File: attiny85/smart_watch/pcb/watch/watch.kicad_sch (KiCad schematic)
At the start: 20 parts, among them J1 Display, J2 USB C, SW1 Wake, SW2 Select, SW3 Set, SW4 Reset, U1 ATTINY85, U2 MCP73831-2-OT

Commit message: production files
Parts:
- removed BT1: Battery_Cell, Battery:BatteryHolder_Keystone_1058_1x2032, symbol Device:Battery_Cell
- added BT1: 1059, BatteryHolder_Keystone_1059_THT:BatteryHolder_Keystone_1059_THT, symbol BatteryHolder_Keystone_1059:1059
- added J3: LiPo Batt, Connector_JST:JST_PH_S2B-PH-K_1x02_P2.00mm_Horizontal, symbol Connector:Conn_01x02_Pin
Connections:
- net GND: now also BT1.N, J3.2 (Pin_2)
- net VCC: now also BT1.P1, J3.1 (Pin_1)
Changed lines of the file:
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@@
+		)
+	)
+	(global_label "GND"
+		(shape bidirectional)
+		(at 105.5509 99.8584 270)
+		(effects
+			(font
+				(size 0.7 0.7)
+			)
+			(justify right)
+		)
+		(property "Intersheetrefs" "${INTERSHEET_REFS}"
+			(at 105.5509 99.8584 0)
+			(effects
+				(font
+					(size 1.27 1.27)
+				)
+				(hide yes)
+			)
 		)
 	)
@@
 		)
 	)
+	(global_label "GND"
+		(shape bidirectional)
+		(at 115.57 95.25 90)
+		(effects
+			(font
+				(size 0.7 0.7)
+			)
+			(justify left)
+		)
+		(property "Intersheetrefs" "${INTERSHEET_REFS}"
+			(at 115.57 95.25 90)
+			(effects
+				(font
+					(size 1.27 1.27)
+				)
+				(hide yes)
+			)
+		)
+	)
 	(global_label "WAKE"
 		(shape output)
@@
 		)
 	)
+	(global_label "VCC"
+		(shape bidirectional)
+		(at 105.556 93.8939 90)
+		(effects
+			(font
+				(size 0.7 0.7)
+			)
+			(justify left)
+		)
+		(property "Intersheetrefs" "${INTERSHEET_REFS}"
+			(at 105.556 93.8939 0)
+			(effects
+				(font
+					(size 1.27 1.27)
+				)
+				(hide yes)
+			)
+		)
+	)
 	(global_label "GND"
 		(shape bidirectional)
@@
 		)
 	)
-	(global_label "VCC"
-		(shape bidirectional)
-		(at 106.68 92.71 90)
-		(effects
-			(font
-				(size 0.7 0.7)
-			)
-			(justify left)
-		)
-		(property "Intersheetrefs" "${INTERSHEET_REFS}"
-			(at 106.68 92.71 0)
-			(effects
-				(font
-					(size 1.27 1.27)
-				)
-				(hide yes)
-			)
-		)
-	)
 	(global_label "SELECT"
 		(shape input)
@@
 		(property "Intersheetrefs" "${INTERSHEET_REFS}"
 			(at 153.67 81.28 0)
-			(effects
-				(font
-					(size 1.27 1.27)
-				)
-				(hide yes)
-			)
-		)
-	)
-	(global_label "GND"
-		(shape bidirectional)
-		(at 106.68 100.33 270)
-		(effects
-			(font
-				(size 0.7 0.7)
-			)
-			(justify right)
-		)
-		(property "Intersheetrefs" "${INTERSHEET_REFS}"
-			(at 106.68 100.33 0)
 			(effects
 				(font
@@
 				)
 				(justify left)
+				(hide yes)
+			)
+		)
+	)
+	(global_label "VCC"
+		(shape bidirectional)
+		(at 113.03 95.25 90)
+		(effects
+			(font
+				(size 0.7 0.7)
+			)
+			(justify left)
+		)
+		(property "Intersheetrefs" "${INTERSHEET_REFS}"
+			(at 113.03 95.25 90)
+			(effects
+				(font
+					(size 1.27 1.27)
+				)
 				(hide yes)
 			)
@@
 	)
 	(symbol
+		(lib_id "BatteryHolder_Keystone_1059:1059")
+		(at 105.556 97.7039 270)
+		(unit 1)
+		(exclude_from_sim no)
+		(in_bom yes)
+		(on_board yes)
+		(dnp yes)
+		(property "Reference" "BT1"
+			(at 97.428 95.4179 90)
+			(effects
+				(font
+					(size 1.27 1.27)
+				)
+				(justify left)
+			)
+		)
+		(property "Value" "1059"
+			(at 97.428 97.9579 90)
+			(effects
+				(font
+					(size 1.27 1.27)
+				)
+				(justify left)
+			)
+		)
+		(property "Footprint" "BatteryHolder_Keystone_1059_THT:BatteryHolder_Keystone_1059_THT"
+			(at 94.888 97.4499 0)
+			(effects
+				(font
+					(size 1.27 1.27)
+				)
+				(justify bottom)
+				(hide yes)
+			)
+		)
+		(property "Datasheet" ""
+			(at 105.556 97.7039 0)
+			(effects
+				(font
+					(size 1.27 1.27)
+				)
+				(hide yes)
+			)
+		)
+		(property "Description" "Keystone Electronics Coin Cell holder 1059"
+			(at 98.698 95.4179 0)
+			(effects
+				(font
+					(size 1.27 1.27)
+				)
+				(hide yes)
+			)
+		)
+		(pin "N"
+		)
+		(pin "P1"
+		)
+		(pin "P2"
+		)
+		(instances
+			(project ""
+				(path "/552443dc-5cb6-43cc-861c-1c1d9f5bdc51"
+					(reference "BT1")
+					(unit 1)
+				)
+			)
+		)
+	)
+	(symbol
 		(lib_id "Device:R")
 		(at 127 133.35 180)
@@
 	)
 	(symbol
-		(lib_id "Device:Battery_Cell")
-		(at 106.68 97.79 0)
-		(unit 1)
-		(exclude_from_sim no)
-		(in_bom yes)
-		(on_board yes)
-		(dnp no)
-		(fields_autoplaced yes)
-		(property "Reference" "BT1"
-			(at 110.49 94.6784 0)
-			(effects
-				(font
-					(size 1.27 1.27)
-				)
-				(justify left)
-			)
-		)
-		(property "Value" "Battery_Cell"
-			(at 110.49 97.2184 0)
-			(effects
-				(font
-					(size 1.27 1.27)
-				)
-				(justify left)
-			)
-		)
-		(property "Footprint" "Battery:BatteryHolder_Keystone_1058_1x2032"
-			(at 106.68 96.266 90)
-			(effects
-				(font
-					(size 1.27 1.27)
-				)
-				(hide yes)
-			)
-		)
-		(property "Datasheet" "~"
-			(at 106.68 96.266 90)
-			(effects
-				(font
-					(size 1.27 1.27)
-				)
-				(hide yes)
-			)
-		)
-		(property "Description" "Single-cell battery"
-			(at 106.68 97.79 0)
-			(effects
-				(font
-					(size 1.27 1.27)
-				)
-				(hide yes)
-			)
-		)
-		(pin "2"
-		)
-		(pin "1"
-		)
-		(instances
-			(project ""
-				(path "/552443dc-5cb6-43cc-861c-1c1d9f5bdc51"
-					(reference "BT1")
-					(unit 1)
-				)
-			)
-		)
-	)
-	(symbol
 		(lib_id "Connector:USB_C_Receptacle_PowerOnly_6P")
 		(at 151.13 124.46 0)
@@
 					(unit 1)
 				)
+			)
+		)
+	)
+	(symbol
+		(lib_id "Connector:Conn_01x02_Pin")
+		(at 113.03 100.33 90)
+		(unit 1)
+		(exclude_from_sim no)
+		(in_bom yes)
+		(on_board yes)
+		(dnp yes)
+		(property "Reference" "J3"
+			(at 114.1866 101.758 90)
+			(effects
+				(font
+					(size 1.27 1.27)
+				)
+			)
+		)
+		(property "Value" "LiPo Batt"
+			(at 114.046 104.394 90)
+			(effects
+				(font
+					(size 1.27 1.27)
+				)
+			)
+		)
+		(property "Footprint" "Connector_JST:JST_PH_S2B-PH-K_1x02_P2.00mm_Horizontal"
+			(at 113.03 100.33 0)
+			(effects
+				(font
+					(size 1.27 1.27)
+				)
+				(hide yes)
+			)
+		)
+		(property "Datasheet" "~"
+			(at 113.03 100.33 0)
+			(effects
+				(font
+					(size 1.27 1.27)
+				)
+				(hide yes)
+			)
+		)
+		(property "Description" "Generic connector, single row, 01x02, script generated"
+			(at 113.03 100.33 0)
+			(effects
+				(font
+					(size 1.27 1.27)
+				)
+				(hide yes)
+			)
+		)
+		(pin "2"
+		)
+		(pin "1"
+		)
+		(instances
+			(project ""
+				(path "/552443dc-5cb6-43cc-861c-1c1d9f5bdc51"
+					(reference "J3")
+					(unit 1)
+				)

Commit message: added programming connection
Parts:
- removed BT1: 1059, BatteryHolder_Keystone_1059_THT:BatteryHolder_Keystone_1059_THT, symbol BatteryHolder_Keystone_1059:1059
- removed J3: LiPo Batt, Connector_JST:JST_PH_S2B-PH-K_1x02_P2.00mm_Horizontal, symbol Connector:Conn_01x02_Pin
- added BT1: Battery_Cell, Battery:BatteryHolder_Keystone_1060_1x2032, symbol Device:Battery_Cell
- added J3: Programmer, JST_PH_1x06_2mm_horizontal:JST_PH_1x06_2mm_horizontal.pretty, symbol JST_PH_1x06_2mm_horizontal:S6B-PH-SM4-TB_LF__SN_
- added P1: JST_LIPO, JST_PH_1x02_2mm_horizontal:JST_PH_1x02_2mm_horizontal, symbol JST_PH_1x02_2mm_horizontal:S2B-PH-SM4-TB_LF__SN_
- R3: value 3.6k -> 6.8k
- SW1, SW2, SW3, SW4: footprint Button_Switch_THT:SW_TH_Tactile_Omron_B3F-100x -> Button_Switch_SMD:SW_SPST_Omron_B3FS-101xP
- U1: footprint Package_DIP:DIP-8_W7.62mm -> Package_DIP:DIP-8_W7.62mm_SMDSocket_SmallPads
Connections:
- net GND: now also BT1.2 (-), J3.5, P1.2
- net RESET: now also J3.6
- net SCK: now also J3.4
- net VCC: now also BT1.1 (+), J3.1, P1.1
- net SDA renamed MOSI
- net MOSI: now also J3.3
- net WAKE renamed MISO
- net MISO: now also J3.2
- new net: J3.S1 (SHIELD), J3.S2 (SHIELD)
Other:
- note added: "Programming"

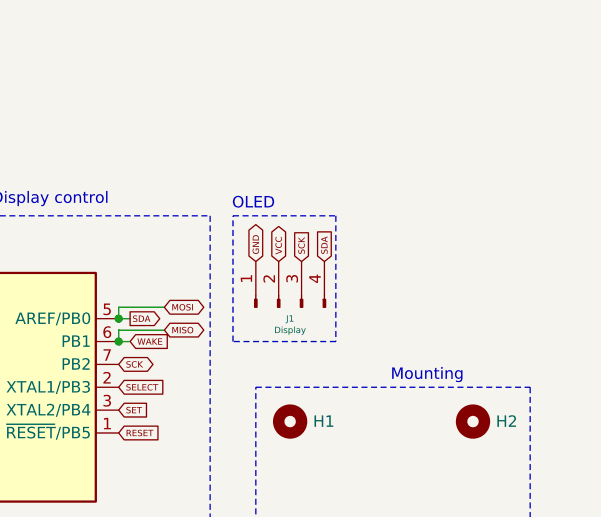
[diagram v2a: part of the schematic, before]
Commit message: watch with straps
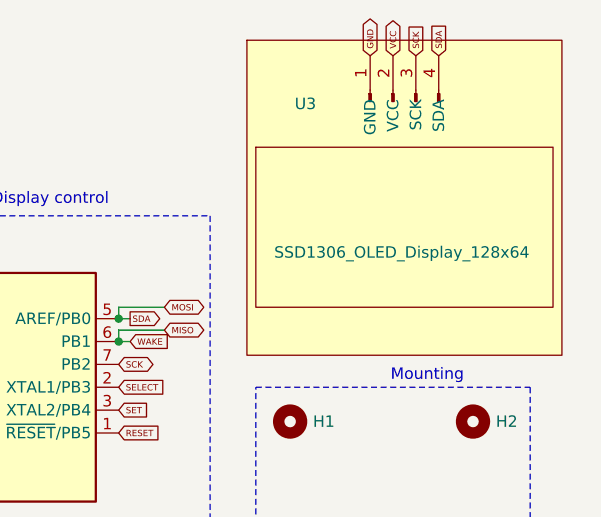
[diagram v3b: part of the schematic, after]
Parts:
- removed J1: Display, Connector_PinHeader_2.54mm:PinHeader_1x04_P2.54mm_Vertical, symbol Connector:Conn_01x04_Pin
- added U3: SSD1306_OLED_Display_128x64, My_Footprints:SSD1306_OLED_Display_128x64, symbol My_Symbols:SSD1306_OLED_Display_128x64
- H1, H2, H3, H4: footprint MountingHole:MountingHole_2.1mm -> My_Footprints:Circular_Mounting_Hole_1mmDia
- J2: footprint Connector_USB:USB_C_Receptacle_HRO_TYPE-C-31-M-17 -> Connector_USB:USB_C_Receptacle_GCT_USB4125-xx-x-0190_6P_TopMnt_Horizontal
- SW1, SW2, SW3, SW4: footprint Button_Switch_SMD:SW_SPST_Omron_B3FS-101xP -> Button_Switch_SMD:SW_Tactile_SPST_NO_Straight_CK_PTS636Sx25SMTRLFS
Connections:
- net GND: now also U3.1 (GND)
- net MOSI: now also U3.4 (SDA)
- net SCK: now also U3.3 (SCK)
- net VCC: now also U3.2 (VCC)
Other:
- note removed: "OLED"
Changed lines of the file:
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@@
-	)
-	(rectangle
-		(start 166.37 62.23)
-		(end 177.8 76.2)
-		(stroke
-			(width 0)
-			(type dash)
-		)
-		(fill
-			(type none)
-		)
 	)
 	(rectangle
@@
 		)
 	)
-	(text "OLED"
-		(exclude_from_sim no)
-		(at 168.656 60.96 0)
-		(effects
-			(font
-				(size 1.27 1.27)
-			)
-		)
-	)
 	(text "MCU: Clock and Display control"
 		(exclude_from_sim no)
@@
 		)
 	)
-	(global_label "SDA"
-		(shape input)
-		(at 176.53 67.31 90)
-		(effects
-			(font
-				(size 0.7 0.7)
-			)
-			(justify left)
-		)
-		(property "Intersheetrefs" "${INTERSHEET_REFS}"
-			(at 176.53 67.31 0)
-			(effects
-				(font
-					(size 1.27 1.27)
-				)
-				(hide yes)
-			)
-		)
-	)
 	(global_label "GND"
 		(shape bidirectional)
@@
 		)
 	)
+	(global_label "SCK"
+		(shape input)
+		(at 186.69 44.45 90)
+		(effects
+			(font
+				(size 0.7 0.7)
+			)
+			(justify left)
+		)
+		(property "Intersheetrefs" "${INTERSHEET_REFS}"
+			(at 186.69 44.45 0)
+			(effects
+				(font
+					(size 1.27 1.27)
+				)
+				(hide yes)
+			)
+		)
+	)
 	(global_label "SET"
 		(shape input)
@@
 		(property "Intersheetrefs" "${INTERSHEET_REFS}"
 			(at 173.99 129.54 0)
+			(effects
+				(font
+					(size 1.27 1.27)
+				)
+				(hide yes)
+			)
+		)
+	)
+	(global_label "GND"
+		(shape bidirectional)
+		(at 181.61 44.45 90)
+		(effects
+			(font
+				(size 0.7 0.7)
+				(color 0 0 0 1)
+			)
+			(justify left)
+		)
+		(property "Intersheetrefs" "${INTERSHEET_REFS}"
+			(at 181.61 44.45 0)
 			(effects
 				(font
@@
 		)
 	)
-	(global_label "GND"
-		(shape bidirectional)
-		(at 168.91 67.31 90)
-		(effects
-			(font
-				(size 0.7 0.7)
-				(color 0 0 0 1)
-			)
-			(justify left)
-		)
-		(property "Intersheetrefs" "${INTERSHEET_REFS}"
-			(at 168.91 67.31 0)
-			(effects
-				(font
-					(size 1.27 1.27)
-				)
-				(hide yes)
-			)
-		)
-	)
-	(global_label "SCK"
-		(shape input)
-		(at 173.99 67.31 90)
-		(effects
-			(font
-				(size 0.7 0.7)
-			)
-			(justify left)
-		)
-		(property "Intersheetrefs" "${INTERSHEET_REFS}"
-			(at 173.99 67.31 0)
-			(effects
-				(font
-					(size 1.27 1.27)
-				)
-				(hide yes)
-			)
-		)
-	)
 	(global_label "VCC"
 		(shape bidirectional)
-		(at 171.45 67.31 90)
+		(at 184.15 44.45 90)
 		(effects
 			(font
@@
 		)
 		(property "Intersheetrefs" "${INTERSHEET_REFS}"
-			(at 171.45 67.31 0)
+			(at 184.15 44.45 0)
 			(effects
 				(font
@@
 		(property "Intersheetrefs" "${INTERSHEET_REFS}"
 			(at 173.99 132.08 0)
+			(effects
+				(font
+					(size 1.27 1.27)
+				)
+				(hide yes)
+			)
+		)
+	)
+	(global_label "SDA"
+		(shape input)
+		(at 189.23 44.45 90)
+		(effects
+			(font
+				(size 0.7 0.7)
+			)
+			(justify left)
+		)
+		(property "Intersheetrefs" "${INTERSHEET_REFS}"
+			(at 189.23 44.45 0)
 			(effects
 				(font
@@
 			)
 		)
-		(property "Footprint" "Button_Switch_SMD:SW_SPST_Omron_B3FS-101xP"
+		(property "Footprint" "Button_Switch_SMD:SW_Tactile_SPST_NO_Straight_CK_PTS636Sx25SMTRLFS"
 			(at 111.76 78.74 0)
 			(effects
@@
 			)
 		)
-		(property "Footprint" "Button_Switch_SMD:SW_SPST_Omron_B3FS-101xP"
+		(property "Footprint" "Button_Switch_SMD:SW_Tactile_SPST_NO_Straight_CK_PTS636Sx25SMTRLFS"
 			(at 111.76 73.66 0)
 			(effects
@@
 			)
 		)
-		(property "Footprint" "MountingHole:MountingHole_2.1mm"
+		(property "Footprint" "My_Footprints:Circular_Mounting_Hole_1mmDia"
 			(at 172.72 99.06 0)
 			(effects
@@
 	)
 	(symbol
+		(lib_id "My_Symbols:SSD1306_OLED_Display_128x64")
+		(at 185.42 45.72 0)
+		(unit 1)
+		(exclude_from_sim no)
+		(in_bom yes)
+		(on_board yes)
+		(dnp no)
+		(property "Reference" "U3"
+			(at 173.228 49.784 0)
+			(effects
+				(font
+					(size 1.27 1.27)
+				)
+				(justify left)
+			)
+		)
+		(property "Value" "SSD1306_OLED_Display_128x64"
+			(at 170.942 66.294 0)
+			(effects
+				(font
+					(size 1.27 1.27)
+				)
+				(justify left)
+			)
+		)
+		(property "Footprint" "My_Footprints:SSD1306_OLED_Display_128x64"
+			(at 185.42 45.72 0)
+			(effects
+				(font
+					(size 1.27 1.27)
+				)
+				(hide yes)
+			)
+		)
+		(property "Datasheet" ""
+			(at 187.325 48.895 90)
+			(effects
+				(font
+					(size 1.27 1.27)
+				)
+				(hide yes)
+			)
+		)
+		(property "Description" "SSD1306 OLED Display with pins"
+			(at 186.436 37.084 0)
+			(effects
+				(font
+					(size 1.27 1.27)
+				)
+				(hide yes)
+			)
+		)
+		(pin "2"
+		)
+		(pin "4"
+		)
+		(pin "3"
+		)
+		(pin "1"
+		)
+		(instances
+			(project ""
+				(path "/552443dc-5cb6-43cc-861c-1c1d9f5bdc51"
+					(reference "U3")
+					(unit 1)
+				)
+			)
+		)
+	)
+	(symbol
 		(lib_id "Device:R")
 		(at 127 133.35 180)
@@
 			)
 		)
-		(property "Footprint" "Button_Switch_SMD:SW_SPST_Omron_B3FS-101xP"
+		(property "Footprint" "Button_Switch_SMD:SW_Tactile_SPST_NO_Straight_CK_PTS636Sx25SMTRLFS"
 			(at 111.76 68.58 0)
 			(effects
@@
 			)
 		)
-		(property "Footprint" "MountingHole:MountingHole_2.1mm"
+		(property "Footprint" "My_Footprints:Circular_Mounting_Hole_1mmDia"
 			(at 193.04 85.09 0)
 			(effects
@@
 			)
 		)
-		(property "Footprint" "Button_Switch_SMD:SW_SPST_Omron_B3FS-101xP"
+		(property "Footprint" "Button_Switch_SMD:SW_Tactile_SPST_NO_Straight_CK_PTS636Sx25SMTRLFS"
 			(at 111.76 63.5 0)
 			(effects
@@
 				(path "/552443dc-5cb6-43cc-861c-1c1d9f5bdc51"
 					(reference "LED1")
-					(unit 1)
-				)
-			)
-		)
-	)
-	(symbol
-		(lib_id "Connector:Conn_01x04_Pin")
-		(at 171.45 72.39 90)
-		(unit 1)
-		(exclude_from_sim no)
-		(in_bom yes)
-		(on_board yes)
-		(dnp no)
-		(fields_autoplaced yes)
-		(property "Reference" "J1"
-			(at 172.72 73.66 90)
-			(effects
-				(font
-					(size 0.7 0.7)
-				)
-			)
-		)
-		(property "Value" "Display"
-			(at 172.72 74.93 90)
-			(effects
-				(font
-					(size 0.7 0.7)
-				)
-			)
-		)
-		(property "Footprint" "Connector_PinHeader_2.54mm:PinHeader_1x04_P2.54mm_Vertical"
-			(at 171.45 72.39 0)
-			(effects
-				(font
-					(size 1.27 1.27)
-				)
-				(hide yes)
-			)
-		)
-		(property "Datasheet" "~"
-			(at 171.45 72.39 0)
-			(effects
-				(font
-					(size 1.27 1.27)
-				)
-				(hide yes)
-			)
-		)
-		(property "Description" "Generic connector, single row, 01x04, script generated"
-			(at 171.45 72.39 0)
-			(effects
-				(font
-					(size 1.27 1.27)
-				)
-				(hide yes)
-			)
-		)
-		(pin "2"
-		)
-		(pin "4"
-		)
-		(pin "3"
-		)
-		(pin "1"
-		)
-		(instances
-			(project ""
-				(path "/552443dc-5cb6-43cc-861c-1c1d9f5bdc51"
-					(reference "J1")
 					(unit 1)
 				)
@@
 			)
 		)
-		(property "Footprint" "MountingHole:MountingHole_2.1mm"
+		(property "Footprint" "My_Footprints:Circular_Mounting_Hole_1mmDia"
 			(at 172.72 85.09 0)
 			(effects
@@
 			)
 		)
-		(property "Footprint" "MountingHole:MountingHole_2.1mm"
+		(property "Footprint" "My_Footprints:Circular_Mounting_Hole_1mmDia"
 			(at 193.04 99.06 0)
 			(effects
@@
 			)
 		)
-		(property "Footprint" "Connector_USB:USB_C_Receptacle_HRO_TYPE-C-31-M-17"
+		(property "Footprint" "Connector_USB:USB_C_Receptacle_GCT_USB4125-xx-x-0190_6P_TopMnt_Horizontal"
 			(at 154.94 121.92 0)
 			(effects
